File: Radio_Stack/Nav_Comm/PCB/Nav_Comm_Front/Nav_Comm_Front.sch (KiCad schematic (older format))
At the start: 11 parts, among them SW1 Switch, SW2 Encoder

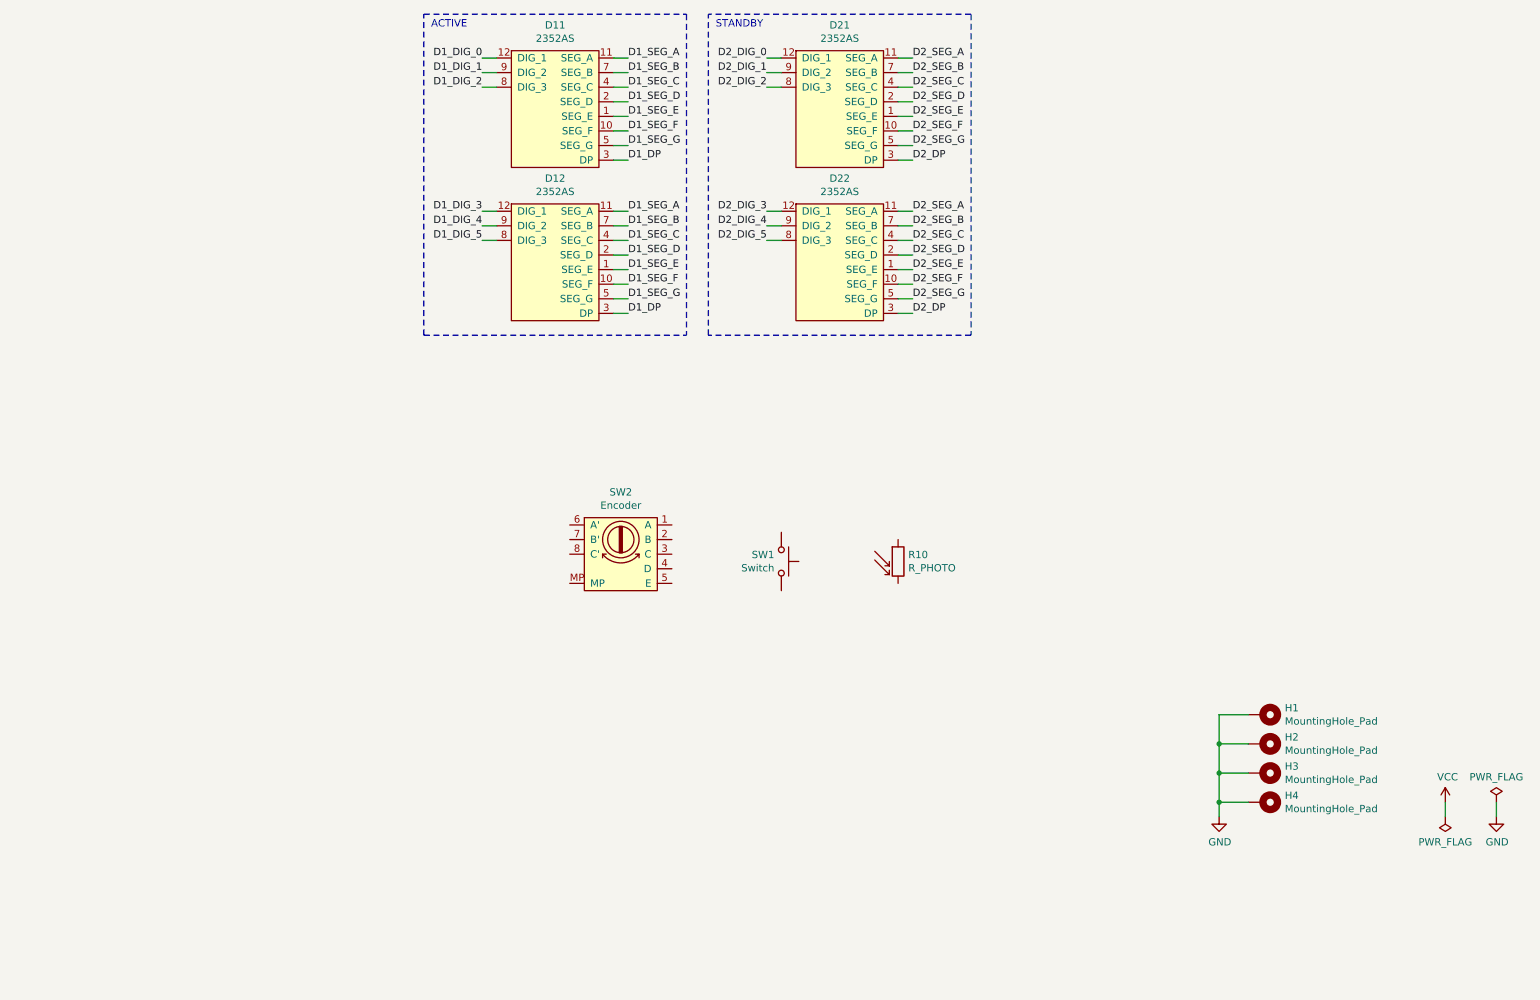
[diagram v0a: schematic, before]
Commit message: custom electronic components 3D models, Nav-Comm module PCB's
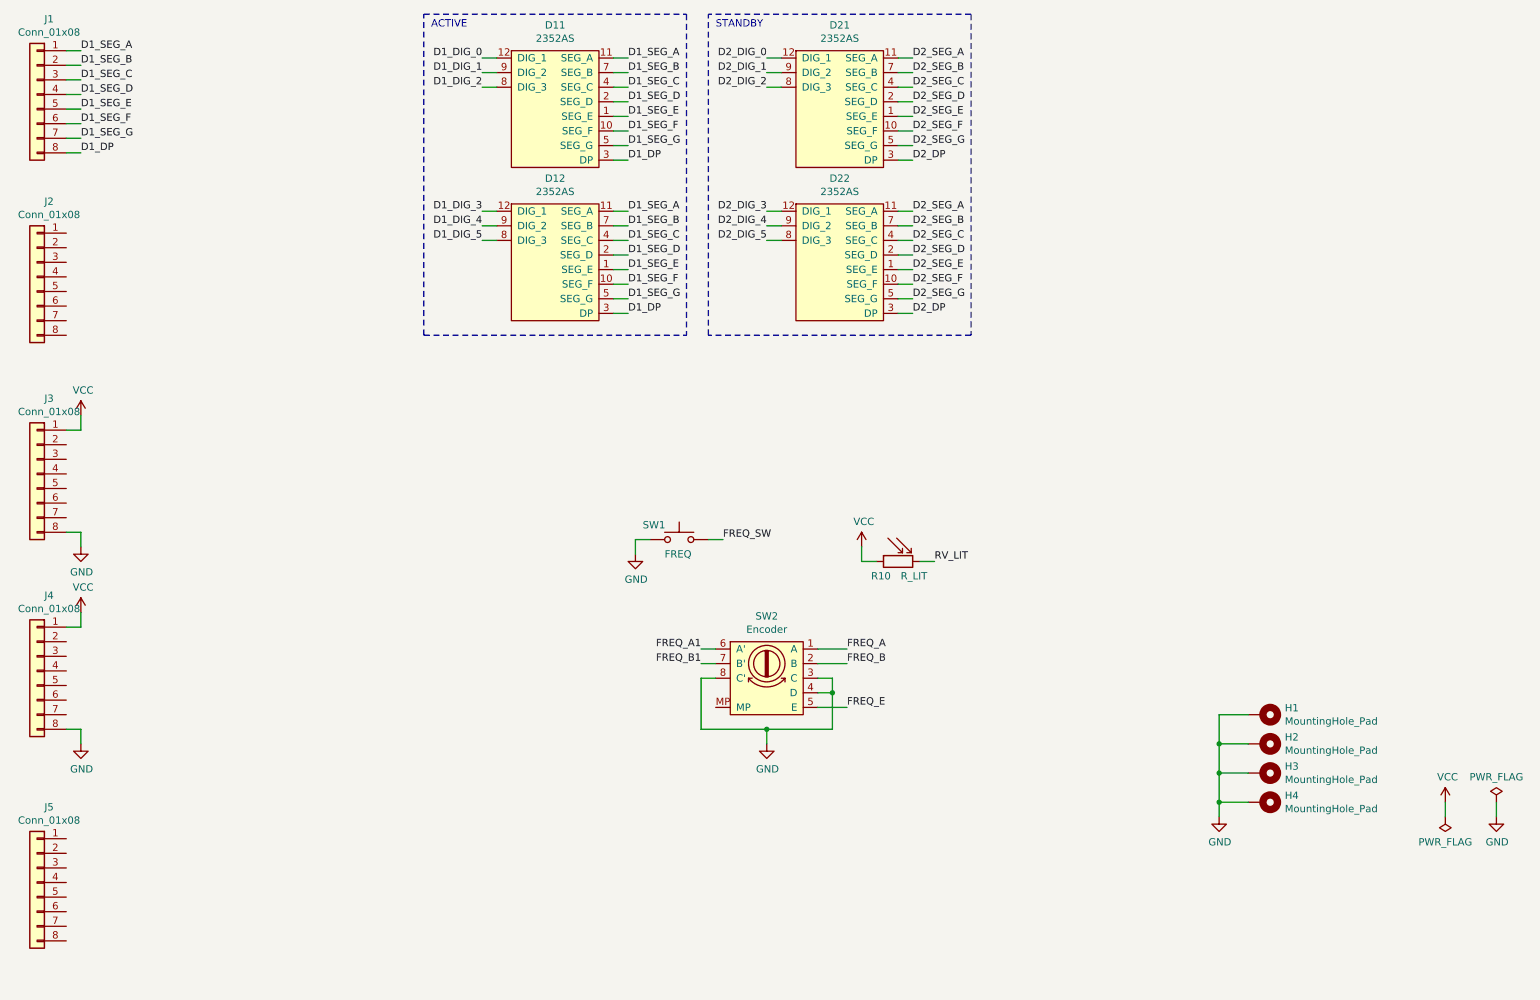
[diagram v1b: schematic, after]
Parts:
- added J1, J2, J3, J4, J5: Conn_01x08, Connector_PinHeader_2.54mm:PinHeader_1x08_P2.54mm_Vertical, symbol Connector_Generic:Conn_01x08
- R10: value R_PHOTO -> R_LIT
- SW1: value Switch -> FREQ
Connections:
- net D1_DP: now also J1.8 (Pin_8)
- net D1_SEG_A: now also J1.1 (Pin_1)
- net D1_SEG_B: now also J1.2 (Pin_2)
- net D1_SEG_C: now also J1.3 (Pin_3)
- net D1_SEG_D: now also J1.4 (Pin_4)
- net D1_SEG_E: now also J1.5 (Pin_5)
- net D1_SEG_F: now also J1.6 (Pin_6)
- net D1_SEG_G: now also J1.7 (Pin_7)
- net GND: now also SW1.2, SW2.3 (C), SW2.4 (D), SW2.8 (C'), J3.8 (Pin_8), J4.8 (Pin_8)
- net VCC: now also R10.1, J3.1 (Pin_1), J4.1 (Pin_1)
- net FREQ_A: now reaches SW2.1 (A)
- net FREQ_B: now reaches SW2.2 (B)
- net FREQ_E: now reaches SW2.5 (E)
- net FREQ_A1: now reaches SW2.6 (A')
- net FREQ_B1: now reaches SW2.7 (B')
- net FREQ_SW: now reaches SW1.1
- net RV_LIT: now reaches R10.2
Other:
- moved on the sheet: R10, SW1, SW2

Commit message: Nav-Comm module PCB's
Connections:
- net D1_DIG_0: now also J3.7 (Pin_7)
- net D1_DIG_1: now also J1.8 (Pin_8)
- net D1_DIG_2: now also J1.7 (Pin_7)
- net D1_DIG_3: now also J1.6 (Pin_6)
- net D1_DIG_4: now also J1.3 (Pin_3)
- net D1_DIG_5: now also J1.2 (Pin_2)
- net D1_DP: now also J3.5 (Pin_5); no longer J1.8 (Pin_8)
- net D1_SEG_A: now also J1.5 (Pin_5); no longer J1.1 (Pin_1)
- net D1_SEG_B: now also J1.1 (Pin_1); no longer J1.2 (Pin_2)
- net D1_SEG_C: now also J3.2 (Pin_2); no longer J1.3 (Pin_3)
- net D1_SEG_D: now also J3.3 (Pin_3); no longer J1.4 (Pin_4)
- net D1_SEG_E: now also J3.6 (Pin_6); no longer J1.5 (Pin_5)
- net D1_SEG_F: now also J1.4 (Pin_4); no longer J1.6 (Pin_6)
- net D1_SEG_G: now also J3.4 (Pin_4); no longer J1.7 (Pin_7)
- net D2_DIG_0: now also J4.7 (Pin_7)
- net D2_DIG_1: now also J2.8 (Pin_8)
- net D2_DIG_2: now also J2.7 (Pin_7)
- net D2_DIG_3: now also J2.6 (Pin_6)
- net D2_DIG_4: now also J2.3 (Pin_3)
- net D2_DIG_5: now also J2.2 (Pin_2)
- net D2_DP: now also J4.5 (Pin_5)
- net D2_SEG_A: now also J2.5 (Pin_5)
- net D2_SEG_B: now also J2.1 (Pin_1)
- net D2_SEG_C: now also J4.2 (Pin_2)
- net D2_SEG_D: now also J4.3 (Pin_3)
- net D2_SEG_E: now also J4.6 (Pin_6)
- net D2_SEG_F: now also J2.4 (Pin_4)
- net D2_SEG_G: now also J4.4 (Pin_4)
- net FREQ_A: now also J5.4 (Pin_4)
- net FREQ_A1: now also J5.1 (Pin_1)
- net FREQ_B: now also J5.5 (Pin_5)
- net FREQ_B1: now also J5.2 (Pin_2)
- net FREQ_E: now also J5.3 (Pin_3)
- net FREQ_SW: now also J5.6 (Pin_6)
- net GND: now also J5.8 (Pin_8)
- net RV_LIT: now also J5.7 (Pin_7)
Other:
- moved on the sheet: D11, D12, D21, D22, J2, J3, J4, R10, SW1, SW2

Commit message: custom electronic components KiCAD symbols, custom electronic components KiCAD footprints, Nav-Comm module PCB's
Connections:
- net GND: now also SW2.MP
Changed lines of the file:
@@
 	5100 5200 5000 5200
-Wire Wire Line
-	5000 5200 5000 5550
 Wire Wire Line
 	5000 5550 5450 5550
@@
 Text Label 1250 5400 0    50   ~ 0
 D2_DIG_0
+Wire Wire Line
+	5100 5400 5000 5400
+Connection ~ 5000 5400
+Wire Wire Line
+	5000 5400 5000 5550
+Wire Wire Line
+	5000 5200 5000 5400
 $EndSCHEMATC
